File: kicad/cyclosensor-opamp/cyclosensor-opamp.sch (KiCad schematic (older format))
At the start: 12 parts, among them J1 RJ14, U1 TCRT5000, U2 MCP6001

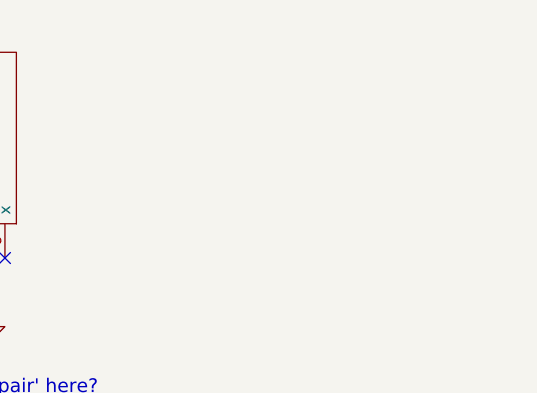
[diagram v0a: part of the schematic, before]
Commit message: tweaks to the opamp-opamp circuit.  remove extra unused stuff.  about ready to move to the layout stage.
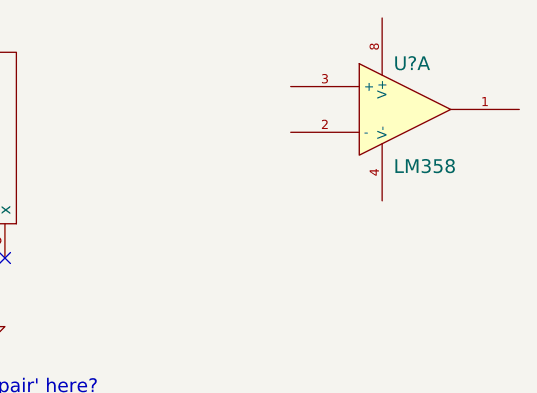
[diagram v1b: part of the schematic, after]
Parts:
- added U?: LM358, symbol LM358
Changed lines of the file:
@@
 Sheet 1 1
 Title ""
-Date "19 apr 2014"
+Date "25 apr 2014"
 Rev ""
 Comp ""
@@
 Text Notes 3200 5850 0    60   ~ 0
 make sure this works without a pot installed.  \nI guess through hole resistor??
+$Comp
+L LM358 U?
+U 1 1 535ABDD9
+P 8950 2850
+F 0 "U?" H 8900 3050 60  0000 L CNN
+F 1 "LM358" H 8900 2600 60  0000 L CNN
+F 2 "" H 8950 2850 60  0000 C CNN
+F 3 "" H 8950 2850 60  0000 C CNN
+	1    8950 2850
+	1    0    0    -1
+$EndComp
 $EndSCHEMATC
